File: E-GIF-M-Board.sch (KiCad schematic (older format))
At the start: 0 parts

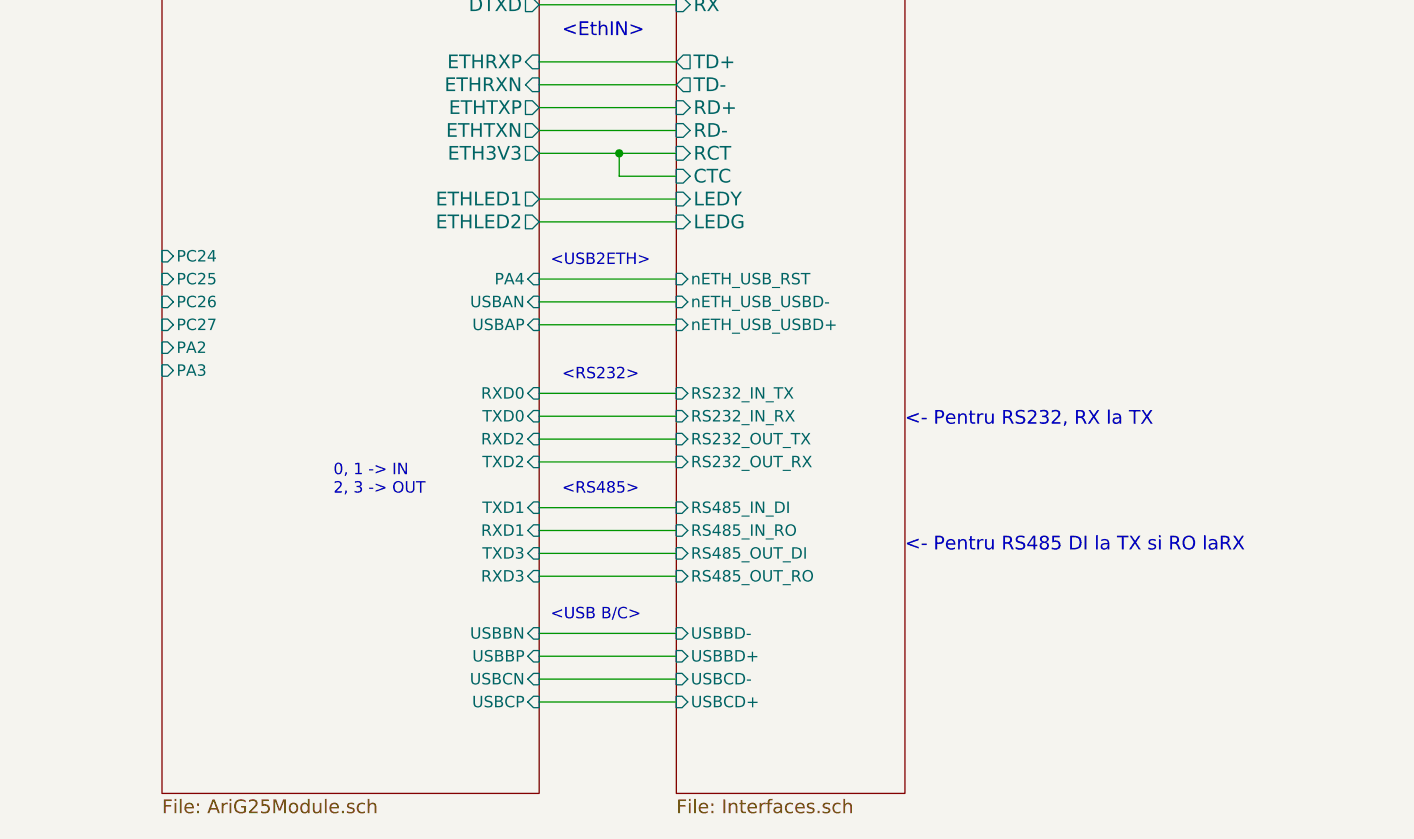
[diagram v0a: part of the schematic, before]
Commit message: Schematic correction
Corrected the direction on some signals. Added a pin header for general development.
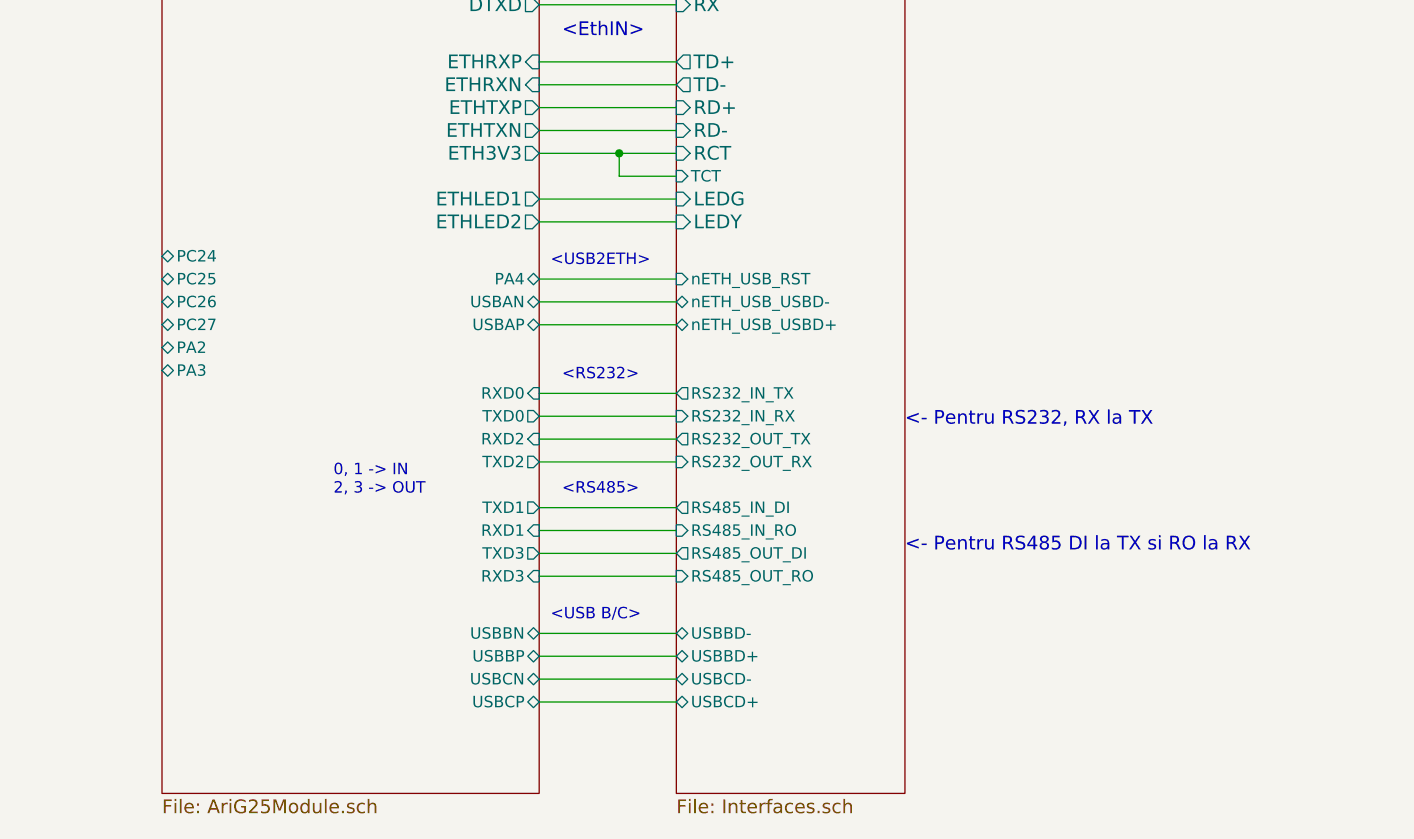
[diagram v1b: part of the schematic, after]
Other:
- note added: "<- Pentru RS485 DI la TX si RO la RX"
- note removed: "<- Pentru RS485 DI la TX si RO laRX"
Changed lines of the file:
@@
 F1 "Power.sch" 60
-$EndSheet
-$Sheet
-S 5650 1100 1650 4500
-U 587D31F1
-F0 "AriaG25Module" 60
-F1 "AriG25Module.sch" 60
-F2 "DA0" B R 7300 1600 60
-F3 "CDA" B R 7300 1700 60
-F4 "CK" O R 7300 1800 60
-F5 "DA1" B R 7300 1500 60
-F6 "DA2" B R 7300 1400 60
-F7 "DA3" B R 7300 1300 60
-F8 "DRXD" I R 7300 2050 60
-F9 "DTXD" O R 7300 2150 60
-F10 "ETHRXP" I R 7300 2400 60
-F11 "ETHRXN" I R 7300 2500 60
-F12 "ETHTXP" O R 7300 2600 60
-F13 "ETHTXN" O R 7300 2700 60
-F14 "ETH3V3" O R 7300 2800 60
-F15 "ETHLED1" O R 7300 3000 60
-F16 "ETHLED2" O R 7300 3100 60
-F17 "RXD2" I R 7300 4050 50
-F18 "TXD2" I R 7300 4150 50
-F19 "RXD1" I R 7300 4450 50
-F20 "TXD1" I R 7300 4350 50
-F21 "RXD0" I R 7300 3850 50
-F22 "TXD0" I R 7300 3950 50
-F23 "TXD3" I R 7300 4550 50
-F24 "RXD3" I R 7300 4650 50
-F25 "USBAP" I R 7300 3550 50
-F26 "USBAN" I R 7300 3450 50
-F27 "PC24" I L 5650 3250 50
-F28 "PC25" I L 5650 3350 50
-F29 "PC26" I L 5650 3450 50
-F30 "PC27" I L 5650 3550 50
-F31 "PA2" I L 5650 3650 50
-F32 "PA3" I L 5650 3750 50
-F33 "PA4" I R 7300 3350 50
-F34 "USBBN" I R 7300 4900 50
-F35 "USBBP" I R 7300 5000 50
-F36 "USBCP" I R 7300 5200 50
-F37 "USBCN" I R 7300 5100 50
-$EndSheet
-$Sheet
-S 7900 1100 1000 4500
-U 587FE94B
-F0 "Interfaces" 60
-F1 "Interfaces.sch" 60
-F2 "DAT2" B L 7900 1400 60
-F3 "DAT3" B L 7900 1300 60
-F4 "CMD" B L 7900 1700 60
-F5 "CLK" I L 7900 1800 60
-F6 "DAT0" B L 7900 1600 60
-F7 "DAT1" B L 7900 1500 60
-F8 "RX" I L 7900 2150 60
-F9 "TX" O L 7900 2050 60
-F10 "RD+" I L 7900 2600 60
-F11 "RCT" I L 7900 2800 60
-F12 "RD-" I L 7900 2700 60
-F13 "TD+" O L 7900 2400 60
-F14 "CTC" I L 7900 2900 60
-F15 "TD-" O L 7900 2500 60
-F16 "LEDG" I L 7900 3100 60
-F17 "LEDY" I L 7900 3000 60
-F18 "nETH_USB_RST" I L 7900 3350 50
-F19 "nETH_USB_USBD-" I L 7900 3450 50
-F20 "nETH_USB_USBD+" I L 7900 3550 50
-F21 "RS232_IN_TX" I L 7900 3850 50
-F22 "RS232_OUT_TX" I L 7900 4050 50
-F23 "RS232_OUT_RX" I L 7900 4150 50
-F24 "RS232_IN_RX" I L 7900 3950 50
-F25 "RS485_IN_DI" I L 7900 4350 50
-F26 "RS485_IN_RO" I L 7900 4450 50
-F27 "RS485_OUT_DI" I L 7900 4550 50
-F28 "RS485_OUT_RO" I L 7900 4650 50
-F29 "USBBD-" I L 7900 4900 50
-F30 "USBBD+" I L 7900 5000 50
-F31 "USBCD-" I L 7900 5100 50
-F32 "USBCD+" I L 7900 5200 50
 $EndSheet
 Text Notes 7350 1250 0    60   ~ 0
@@
 <- Pentru RS232, RX la TX
 Text Notes 8900 4550 0    60   ~ 0
-<- Pentru RS485 DI la TX si RO laRX
+<- Pentru RS485 DI la TX si RO la RX
 Wire Wire Line
 	7300 1300 7900 1300
@@
 Text Notes 7350 4850 0    50   ~ 0
 <USB B/C>
+$Sheet
+S 5650 1100 1650 4500
+U 587D31F1
+F0 "AriaG25Module" 60
+F1 "AriG25Module.sch" 60
+F2 "DA0" B R 7300 1600 60
+F3 "CDA" B R 7300 1700 60
+F4 "CK" O R 7300 1800 60
+F5 "DA1" B R 7300 1500 60
+F6 "DA2" B R 7300 1400 60
+F7 "DA3" B R 7300 1300 60
+F8 "DRXD" I R 7300 2050 60
+F9 "DTXD" O R 7300 2150 60
+F10 "ETHRXP" I R 7300 2400 60
+F11 "ETHRXN" I R 7300 2500 60
+F12 "ETHTXP" O R 7300 2600 60
+F13 "ETHTXN" O R 7300 2700 60
+F14 "ETH3V3" O R 7300 2800 60
+F15 "ETHLED1" O R 7300 3000 60
+F16 "ETHLED2" O R 7300 3100 60
+F17 "RXD2" I R 7300 4050 50
+F18 "RXD1" I R 7300 4450 50
+F19 "RXD0" I R 7300 3850 50
+F20 "RXD3" I R 7300 4650 50
+F21 "USBBN" B R 7300 4900 50
+F22 "USBBP" B R 7300 5000 50
+F23 "USBCN" B R 7300 5100 50
+F24 "USBCP" B R 7300 5200 50
+F25 "TXD1" O R 7300 4350 50
+F26 "TXD3" O R 7300 4550 50
+F27 "TXD0" O R 7300 3950 50
+F28 "TXD2" O R 7300 4150 50
+F29 "USBAN" B R 7300 3450 50
+F30 "USBAP" B R 7300 3550 50
+F31 "PA4" B R 7300 3350 50
+F32 "PC24" B L 5650 3250 50
+F33 "PC25" B L 5650 3350 50
+F34 "PC26" B L 5650 3450 50
+F35 "PC27" B L 5650 3550 50
+F36 "PA2" B L 5650 3650 50
+F37 "PA3" B L 5650 3750 50
+$EndSheet
+$Sheet
+S 7900 1100 1000 4500
+U 587FE94B
+F0 "Interfaces" 60
+F1 "Interfaces.sch" 60
+F2 "DAT2" B L 7900 1400 60
+F3 "DAT3" B L 7900 1300 60
+F4 "CMD" B L 7900 1700 60
+F5 "CLK" I L 7900 1800 60
+F6 "DAT0" B L 7900 1600 60
+F7 "DAT1" B L 7900 1500 60
+F8 "RX" I L 7900 2150 60
+F9 "TX" O L 7900 2050 60
+F10 "RD+" I L 7900 2600 60
+F11 "RCT" I L 7900 2800 60
+F12 "RD-" I L 7900 2700 60
+F13 "TD+" O L 7900 2400 60
+F14 "TD-" O L 7900 2500 60
+F15 "LEDG" I L 7900 3000 60
+F16 "LEDY" I L 7900 3100 60
+F17 "nETH_USB_RST" I L 7900 3350 50
+F18 "TCT" I L 7900 2900 50
+F19 "nETH_USB_USBD-" B L 7900 3450 50
+F20 "nETH_USB_USBD+" B L 7900 3550 50
+F21 "RS232_IN_TX" O L 7900 3850 50
+F22 "RS232_IN_RX" I L 7900 3950 50
+F23 "RS232_OUT_TX" O L 7900 4050 50
+F24 "RS232_OUT_RX" I L 7900 4150 50
+F25 "RS485_IN_DI" O L 7900 4350 50
+F26 "RS485_IN_RO" I L 7900 4450 50
+F27 "RS485_OUT_DI" O L 7900 4550 50
+F28 "RS485_OUT_RO" I L 7900 4650 50
+F29 "USBBD-" B L 7900 4900 50
+F30 "USBBD+" B L 7900 5000 50
+F31 "USBCD-" B L 7900 5100 50
+F32 "USBCD+" B L 7900 5200 50
+$EndSheet
 $EndSCHEMATC

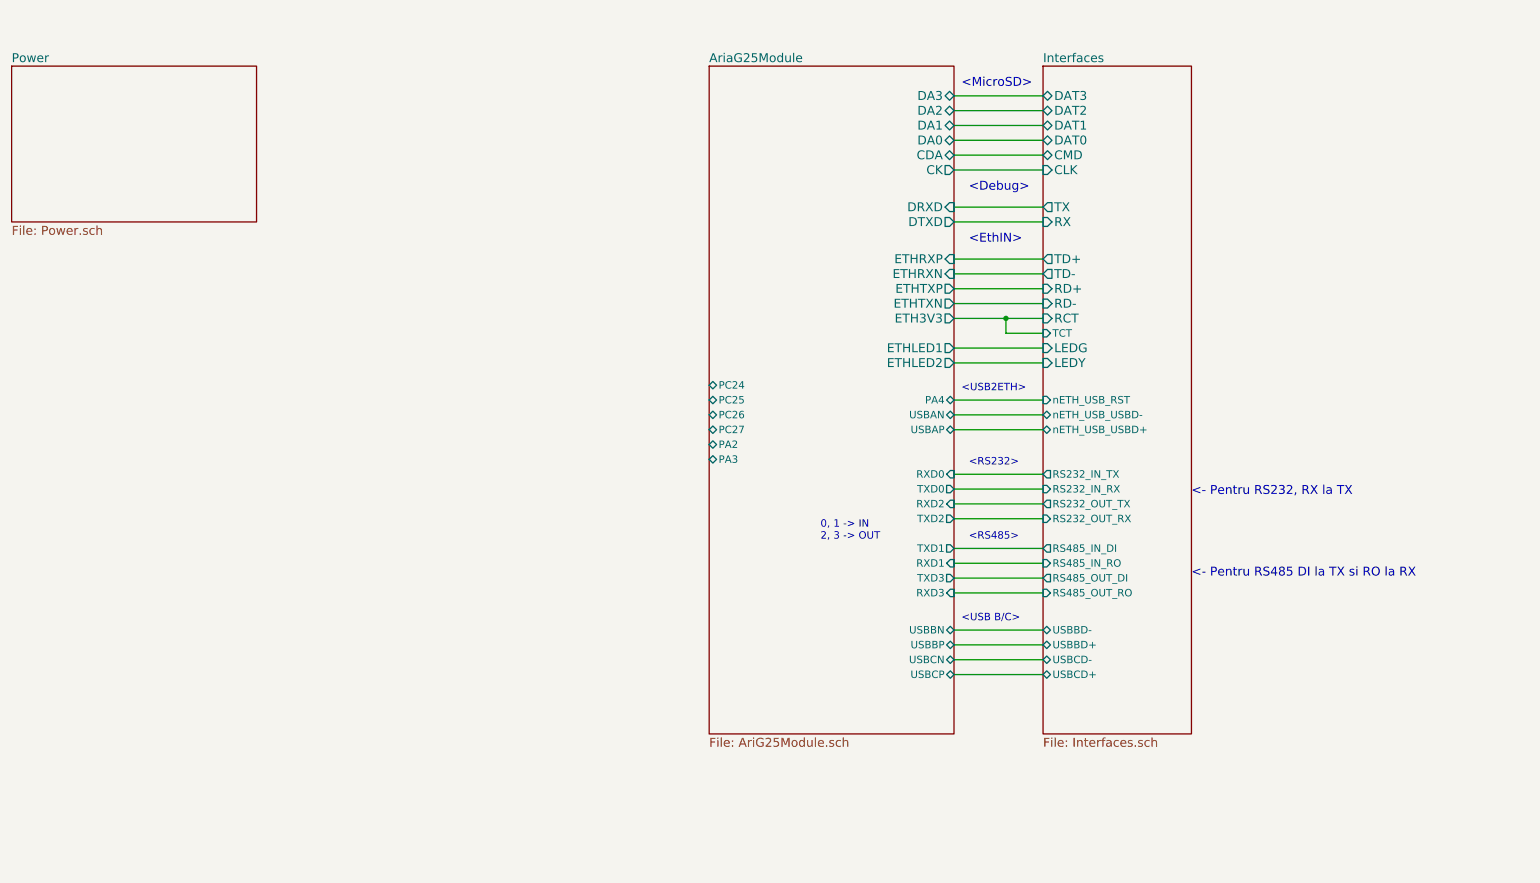
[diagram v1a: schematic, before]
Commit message: Schematic changes. PCB in process of making.
Removed LAN9500A Jtag. Removed Aria G25 pinout. Removed USB connectors. Added rezistors to USB/ETH/ySD shields.
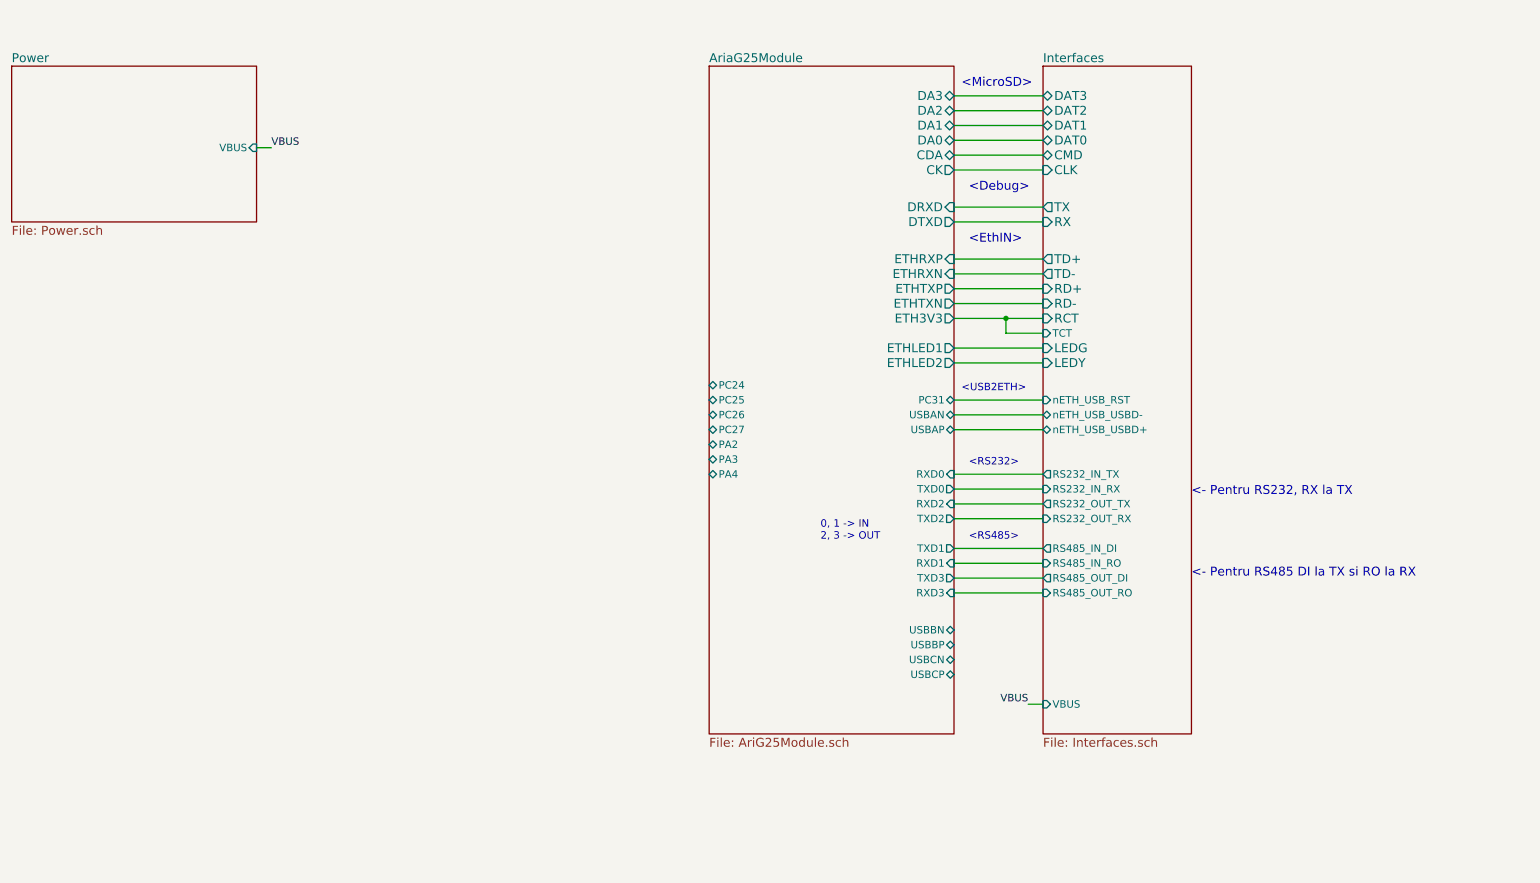
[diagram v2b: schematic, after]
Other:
- note removed: "<USB B/C>"
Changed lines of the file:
@@
 F0 "Power" 60
 F1 "Power.sch" 60
+F2 "VBUS" I R 2600 1650 50
 $EndSheet
 Text Notes 7350 1250 0    60   ~ 0
@@
 Wire Wire Line
 	7300 3550 7900 3550
-Wire Wire Line
-	7300 4900 7900 4900
-Wire Wire Line
-	7300 5000 7900 5000
-Wire Wire Line
-	7300 5100 7900 5100
-Wire Wire Line
-	7300 5200 7900 5200
-Text Notes 7350 4850 0    50   ~ 0
-<USB B/C>
 $Sheet
 S 5650 1100 1650 4500
@@
 F29 "USBAN" B R 7300 3450 50
 F30 "USBAP" B R 7300 3550 50
-F31 "PA4" B R 7300 3350 50
+F31 "PA4" B L 5650 3850 50
 F32 "PC24" B L 5650 3250 50
 F33 "PC25" B L 5650 3350 50
@@
 F36 "PA2" B L 5650 3650 50
 F37 "PA3" B L 5650 3750 50
+F38 "PC31" B R 7300 3350 50
 $EndSheet
 $Sheet
@@
 F27 "RS485_OUT_DI" O L 7900 4550 50
 F28 "RS485_OUT_RO" I L 7900 4650 50
-F29 "USBBD-" B L 7900 4900 50
-F30 "USBBD+" B L 7900 5000 50
-F31 "USBCD-" B L 7900 5100 50
-F32 "USBCD+" B L 7900 5200 50
+F33 "VBUS" I L 7900 5400 50
 $EndSheet
+Text Label 7800 5400 2    50   ~ 0
+VBUS
+Wire Wire Line
+	7800 5400 7900 5400
+Text Label 2700 1650 0    50   ~ 0
+VBUS
+Wire Wire Line
+	2600 1650 2700 1650
 $EndSCHEMATC

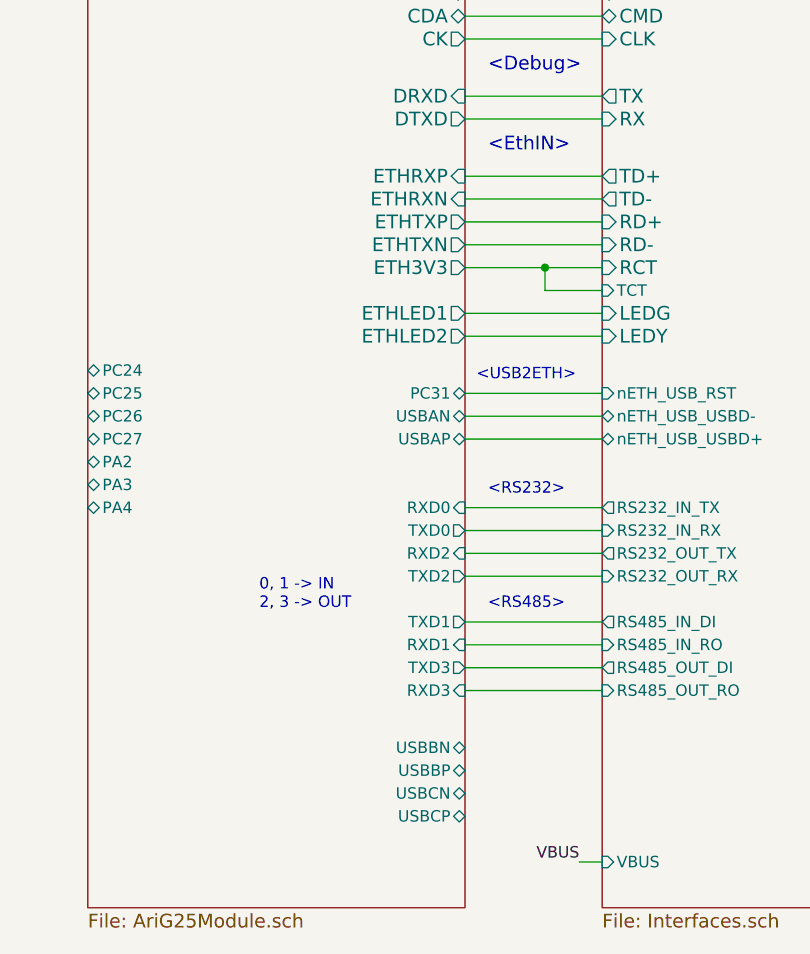
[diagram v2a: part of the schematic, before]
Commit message: Modified USB/ETH label names.
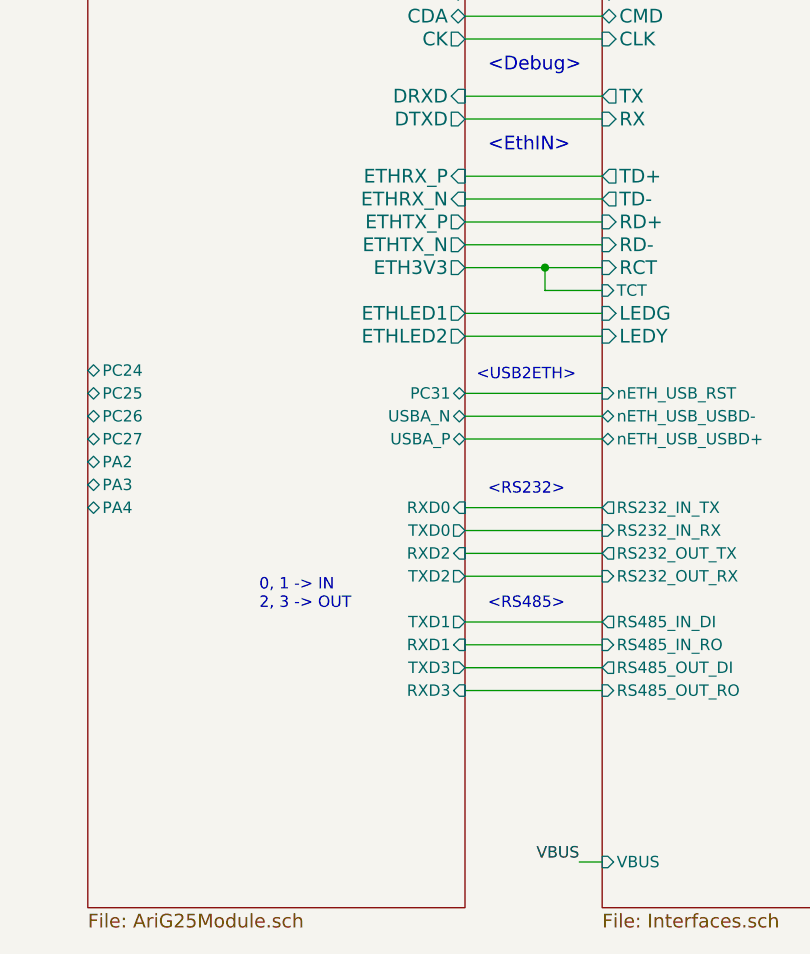
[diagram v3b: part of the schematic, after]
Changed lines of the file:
@@
 F8 "DRXD" I R 7300 2050 60
 F9 "DTXD" O R 7300 2150 60
-F10 "ETHRXP" I R 7300 2400 60
-F11 "ETHRXN" I R 7300 2500 60
-F12 "ETHTXP" O R 7300 2600 60
-F13 "ETHTXN" O R 7300 2700 60
+F10 "ETHRX_P" I R 7300 2400 60
+F11 "ETHRX_N" I R 7300 2500 60
+F12 "ETHTX_P" O R 7300 2600 60
+F13 "ETHTX_N" O R 7300 2700 60
 F14 "ETH3V3" O R 7300 2800 60
 F15 "ETHLED1" O R 7300 3000 60
@@
 F19 "RXD0" I R 7300 3850 50
 F20 "RXD3" I R 7300 4650 50
-F21 "USBBN" B R 7300 4900 50
-F22 "USBBP" B R 7300 5000 50
-F23 "USBCN" B R 7300 5100 50
-F24 "USBCP" B R 7300 5200 50
 F25 "TXD1" O R 7300 4350 50
 F26 "TXD3" O R 7300 4550 50
 F27 "TXD0" O R 7300 3950 50
 F28 "TXD2" O R 7300 4150 50
-F29 "USBAN" B R 7300 3450 50
-F30 "USBAP" B R 7300 3550 50
+F29 "USBA_N" B R 7300 3450 50
+F30 "USBA_P" B R 7300 3550 50
 F31 "PA4" B L 5650 3850 50
 F32 "PC24" B L 5650 3250 50
@@
 F27 "RS485_OUT_DI" O L 7900 4550 50
 F28 "RS485_OUT_RO" I L 7900 4650 50
-F33 "VBUS" I L 7900 5400 50
+F29 "VBUS" I L 7900 5400 50
 $EndSheet
 Text Label 7800 5400 2    50   ~ 0
